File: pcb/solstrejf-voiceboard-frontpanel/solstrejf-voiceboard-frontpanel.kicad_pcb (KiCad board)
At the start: 2 copper layers, 47.8 x 104.6 mm, 13 parts, among them J1 Conn_02x08_Odd_Even, SW1 SW_Push

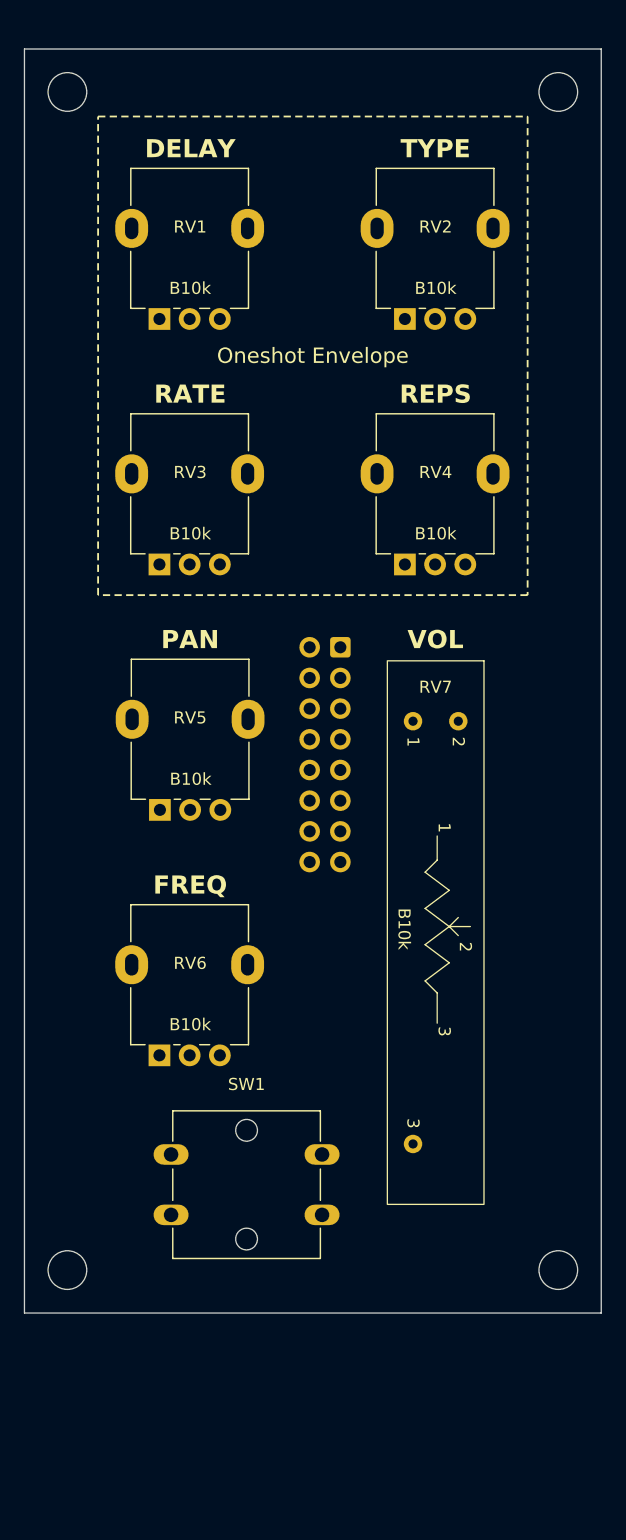
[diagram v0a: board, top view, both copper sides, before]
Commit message: updated Kromftronics submodule name and edited path in all PCB projects. Added work-in-progress for the front-panel PCB and the small updates in the voice-board schematic
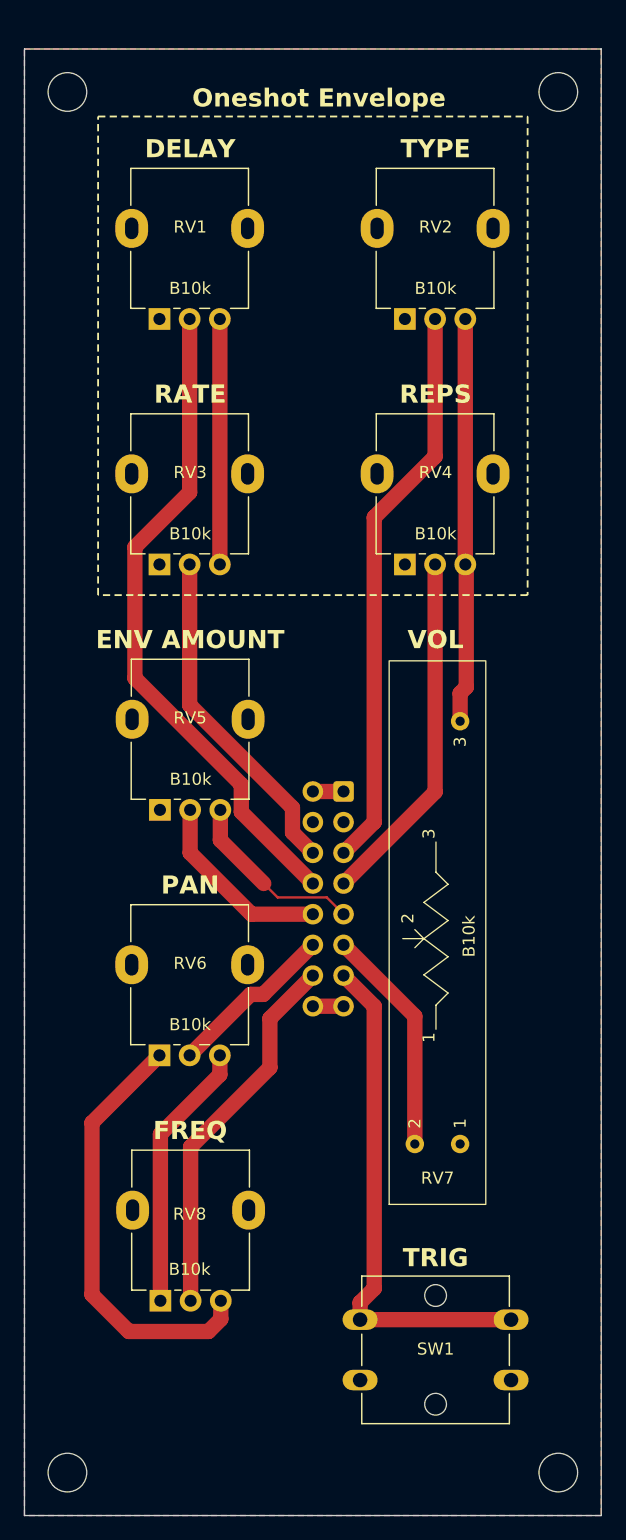
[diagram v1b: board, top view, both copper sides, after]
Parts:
- added RV8: B10k, Potentiometer_THT:Potentiometer_Alpha_RD901F-40-00D_Single_Vertical, F.Cu at (127.1, 149.9)
- SW1: value SW_Push -> TRIG
- moved RV7 35.2 mm to (151.9, 136.9), turned to 90 degrees
- moved SW1 20.8 mm to (143.6, 151.4)
- moved H3 16.8 mm to (119.4, 164.1)
- moved H4 16.8 mm to (160.0, 164.1)
- moved J1 11.9 mm to (142.2, 107.7)
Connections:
- J1 pad 10: /PAN -> /ONESHOT_TO_BOARD
- J1 pad 11: /ONESHOT_TRIG -> /VOL
- J1 pad 12: /FREQ -> /PAN
- J1 pad 13: GND -> /ONESHOT_TRIG
- J1 pad 14: GND -> /FREQ
- J1 pad 6: /ONESHOT_DEL -> /ONESHOT_RATE
- J1 pad 8: /ONESHOT_RATE -> /ONESHOT_DEL
- J1 pad 9: /VOL -> /ONESHOT_FROM_BOARD
- RV1 pad 1: +5V -> GND
- RV1 pad 3: GND -> +5V
- RV2 pad 1: +5V -> GND
- RV2 pad 3: GND -> +5V
- RV3 pad 1: +5V -> GND
- RV3 pad 3: GND -> +5V
- RV4 pad 1: +5V -> GND
- RV4 pad 3: GND -> +5V
- RV5 pad 1: +5V -> GND
- RV5 pad 2: /PAN -> /ONESHOT_TO_BOARD
- RV5 pad 3: -5V -> /ONESHOT_FROM_BOARD
- RV6 pad 1: +5V -> -5V
- RV6 pad 2: /FREQ -> /PAN
- RV6 pad 3: -5V -> +5V
- RV7 pad 1: +5V -> GND
- RV7 pad 3: GND -> +5V
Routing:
- net +5V: track 0.00 -> 78.8 mm
- net /ONESHOT_DEL: track 0.00 -> 54.7 mm
- net /ONESHOT_TYPE: track 0.00 -> 47.3 mm
- net /ONESHOT_TRIG: track 0.00 -> 42.5 mm
- net -5V: track 0.00 -> 38.5 mm
- net /FREQ: track 0.00 -> 31.1 mm
- net /ONESHOT_REPS: track 0.00 -> 29.6 mm
- net /ONESHOT_RATE: track 0.00 -> 28.1 mm
- net /VOL: track 0.00 -> 18.9 mm
- net /ONESHOT_TO_BOARD: track 0.00 -> 15.8 mm
- net /ONESHOT_FROM_BOARD: track 0.00 -> 15.2 mm
- net /PAN: track 0.00 -> 14.0 mm
- added copper zone on B.Cu, net GND
- added copper zone on F.Cu, net GND
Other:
- board size 47.8 x 104.6 mm -> 47.8 x 121.4 mm
- board text added: "+5V"
- board text added: "-5V"
- board text added: "ENV AMOUNT"

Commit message: Updated voice board front-panel and mod-matrix
Created new dimensions to get a better physical layout of the 4x voice board control panels and the mod-matrix.
Exported .wrl 3D models of voice board front-panel and mod-matrix to create a MeshLab view.
Added MeshLab project files and new images aswell.
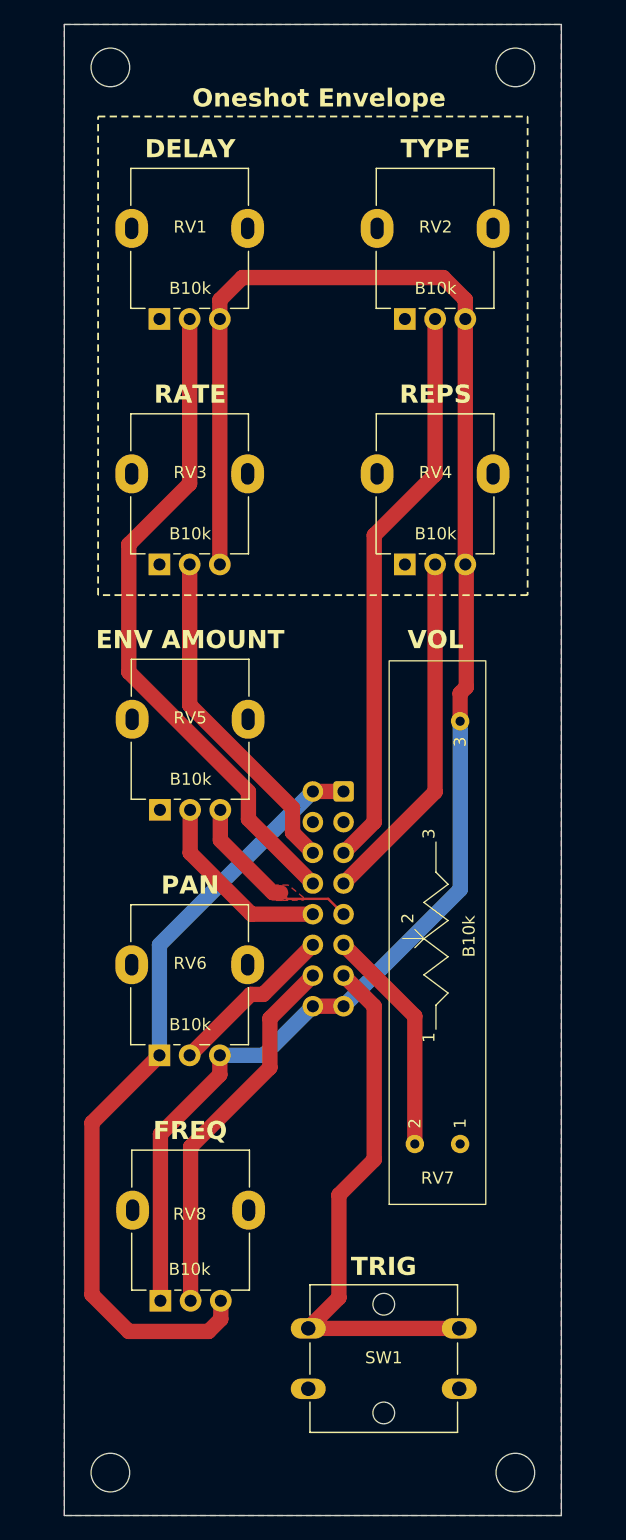
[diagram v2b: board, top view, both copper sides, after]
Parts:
- moved SW1 4.35 mm to (139.3, 152.1)
- moved H1 4.10 mm to (122.9, 47.8)
- moved H2 4.10 mm to (156.5, 47.8)
- moved H3 3.56 mm to (122.9, 164.1)
- moved H4 3.56 mm to (156.5, 164.1)
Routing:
- net +5V: track 78.8 -> 140.8 mm
- net -5V: track 38.5 -> 65.6 mm
- net /ONESHOT_TRIG: track 42.5 -> 45.0 mm
- added copper zone on F.Cu, net /ONESHOT_FROM_BOARD
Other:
- board size 47.8 x 121.4 mm -> 41.1 x 123.4 mm
- board text added: "Solstrejf // Voice Board Control Panel Rev 1.0"

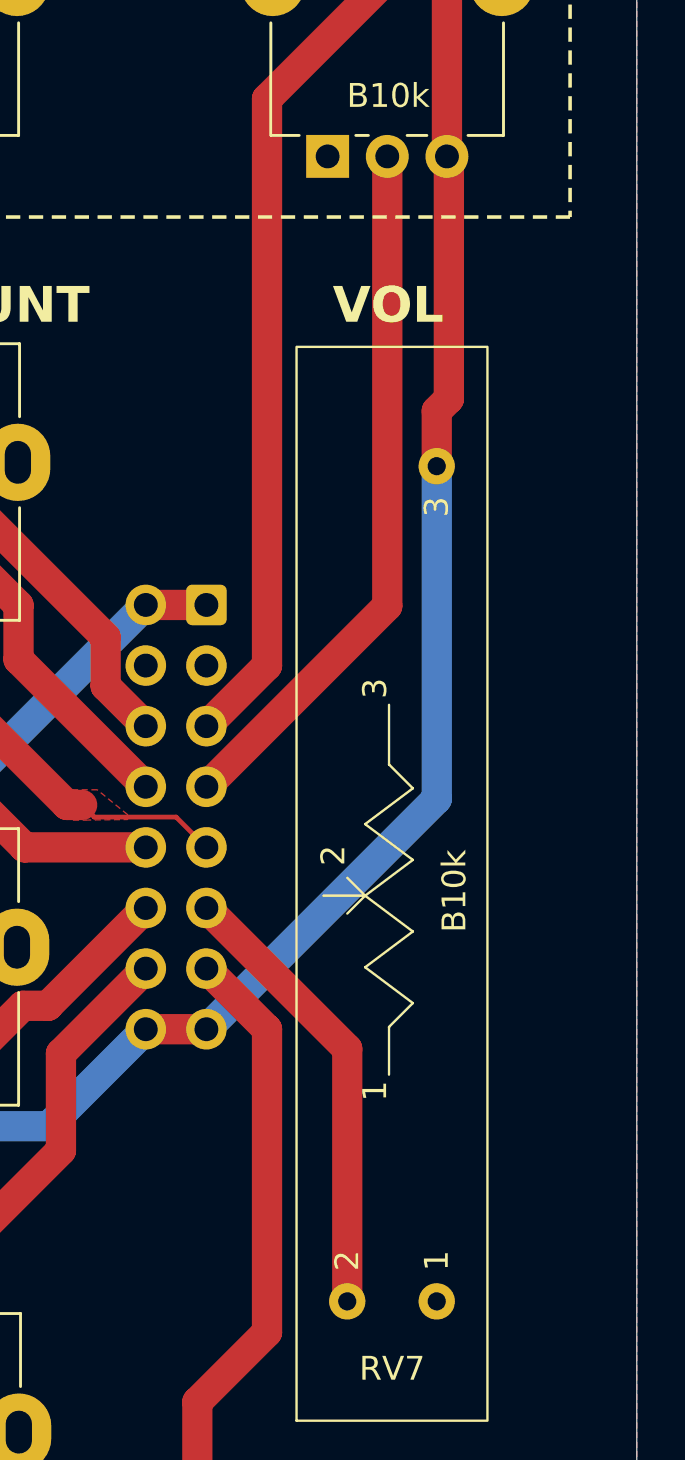
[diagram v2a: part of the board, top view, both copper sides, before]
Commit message: Found an error in the front panel where the volume pot was inverted. Updated the schematics of the voice board core and front panel.
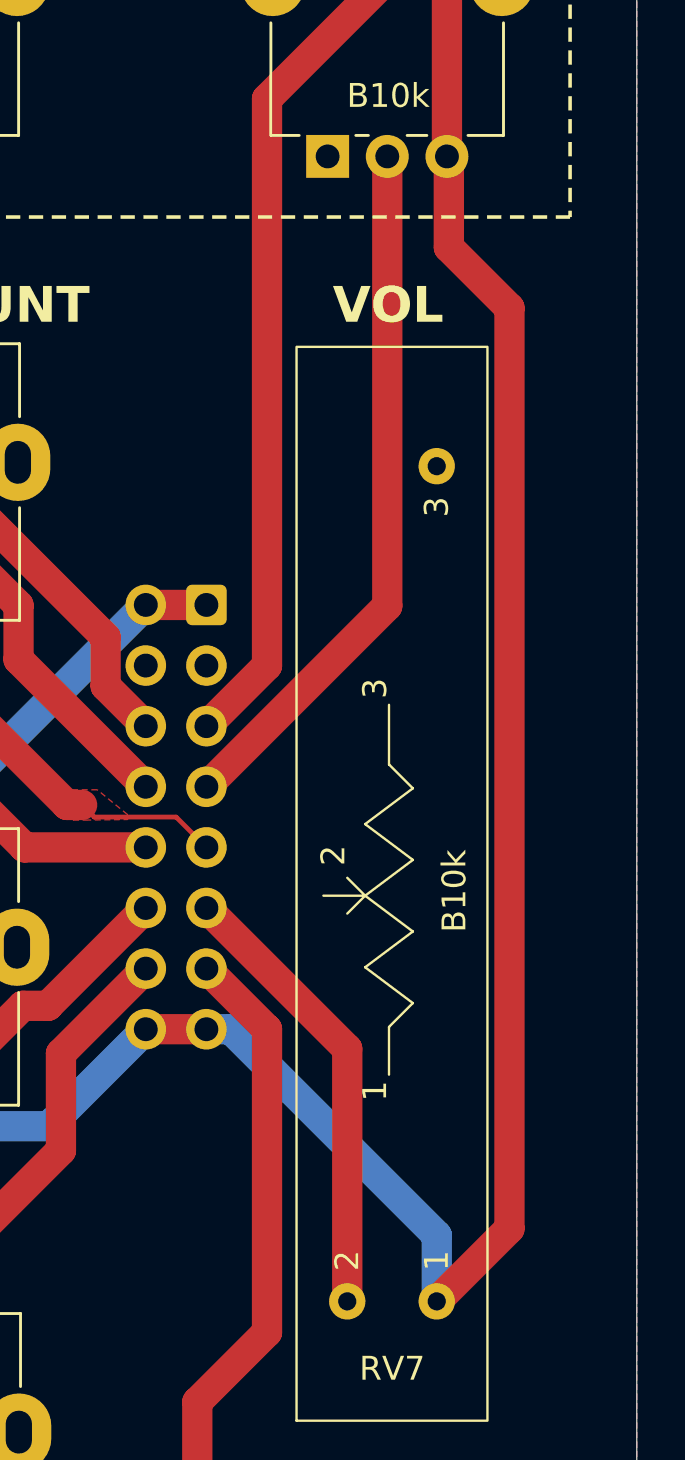
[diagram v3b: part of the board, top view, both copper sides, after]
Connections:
- RV7 pad 1: GND -> +5V
- RV7 pad 3: +5V -> GND
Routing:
- net +5V: track 140.8 -> 166.3 mm
